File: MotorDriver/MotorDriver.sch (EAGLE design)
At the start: 21 parts, among them U1 ATTINY48/88-TQFP, U2 DRV8848

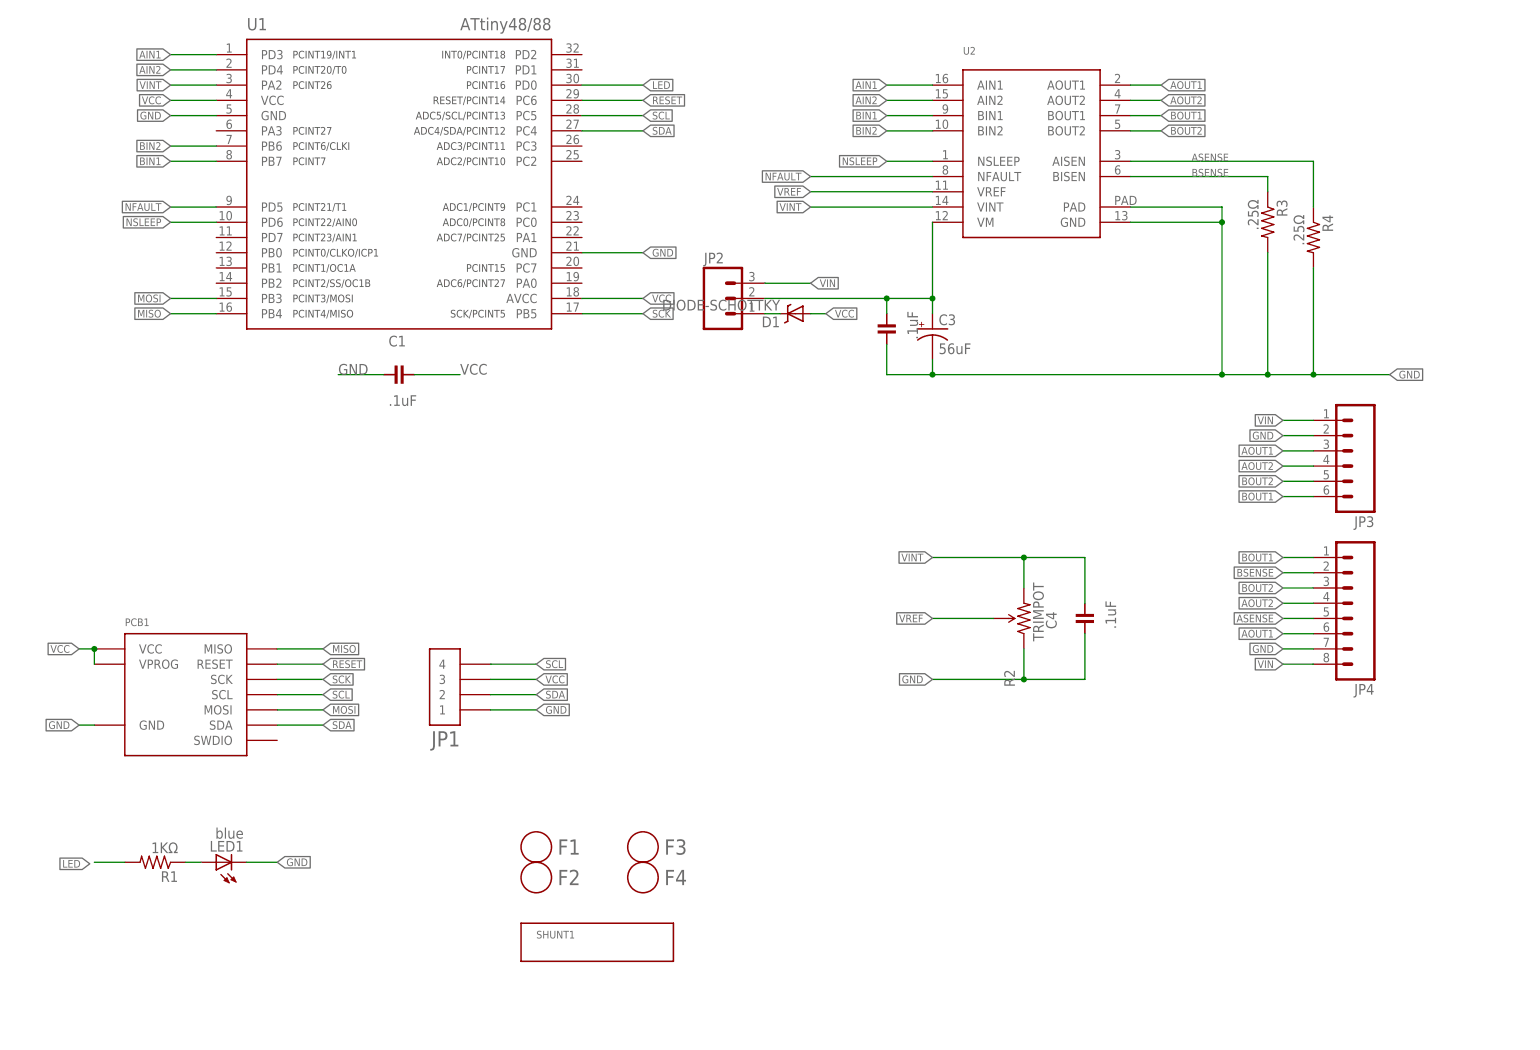
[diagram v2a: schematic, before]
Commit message: Check point of current PCB designs. Among other things I think this change includes rewiring of programming lines on many of the boards,.
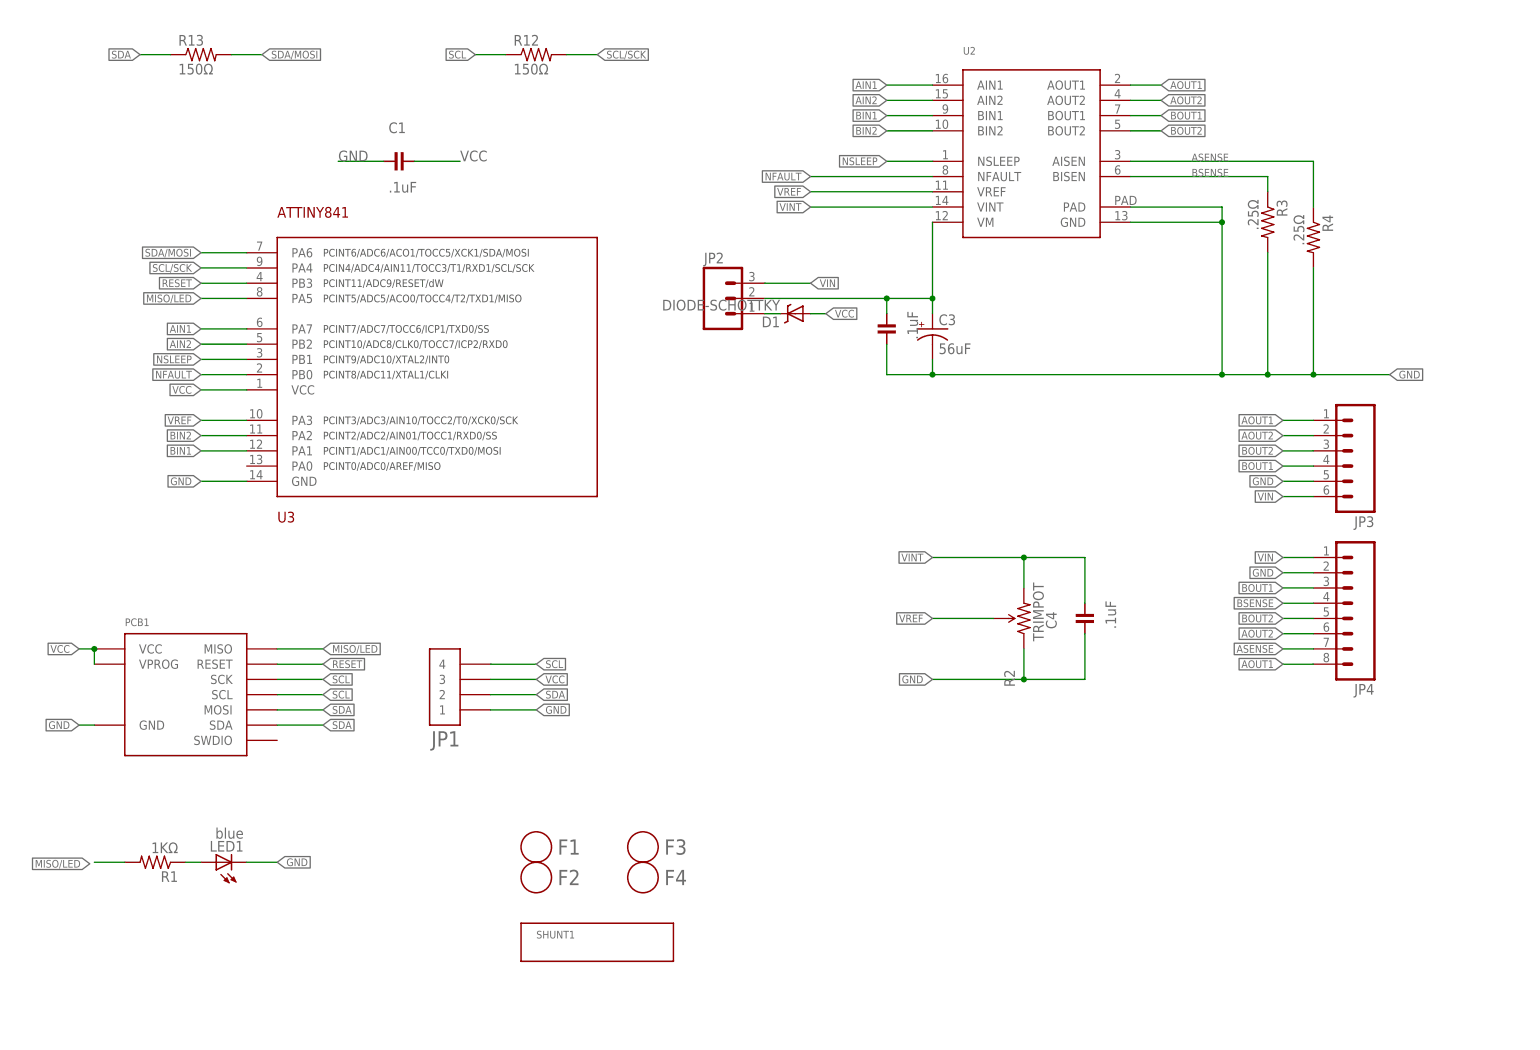
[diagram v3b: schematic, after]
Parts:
- removed U1: ATTINY48/88-TQFP, Modulo:ATTINY48/88-TQFP
- added R12, R13: 150Ω, Modulo:RESISTOR-150Ω
- added U3: ATTINY841, Modulo:ATTINY841
- JP4: BOM (none) -> EXCLUDE
- U2: PARTNUM DRV8848 -> (none)
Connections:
- removed net LED: R1.2, U1.PD0
- removed net MISO: PCB1.MISO, U1.PB4
- removed net MOSI: PCB1.MOSI, U1.PB3
- removed net SCK: PCB1.SCK, U1.PB5
- new net MISO/LED: PCB1.MISO, R1.2, U3.PA5
- new net SCL/SCK: R12.2, U3.PA4
- new net SDA/MOSI: R13.2, U3.PA6
- net AIN1: now also U3.PA7; no longer U1.PD3
- net AIN2: now also U3.PB2; no longer U1.PD4
- net AOUT1: now also JP3.1, JP4.8; no longer JP3.3, JP4.6
- net AOUT2: now also JP3.2, JP4.6; no longer JP3.4, JP4.4
- net ASENSE: now also JP4.7; no longer JP4.5
- net BIN1: now also U3.PA1; no longer U1.PB7
- net BIN2: now also U3.PA2; no longer U1.PB6
- net BOUT1: now also JP3.4, JP4.3; no longer JP3.6, JP4.1
- net BOUT2: now also JP3.3, JP4.5; no longer JP3.5, JP4.3
- net BSENSE: now also JP4.4; no longer JP4.2
- net GND: now also JP3.5, JP4.2, U3.GND; no longer JP3.2, JP4.7, U1.GND, U1.GND@1
- net NFAULT: now also U3.PB0; no longer U1.PD5
- net NSLEEP: now also U3.PB1; no longer U1.PD6
- net RESET: now also U3.PB3; no longer U1.PC6
- net SCL: now also PCB1.SCK, R12.1; no longer U1.PC5
- net SDA: now also PCB1.MOSI, R13.1; no longer U1.PC4
- net VCC: now also U3.VCC; no longer U1.AVCC, U1.VCC
- net VIN: now also JP3.6, JP4.1; no longer JP3.1, JP4.8
- net VINT: no longer U1.PA2
- net VREF: now also U3.PA3
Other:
- moved on the sheet: C1

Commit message: Various changes
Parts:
- removed JP4: (no value), SparkFun-Connectors:M08NO_SILK
- removed R2: TRIMPOT, Modulo:TRIMPOT
- added SJ1, SJ2, SJ3: SOLDERJUMPERNO, SparkFun-Passives:SOLDERJUMPERNO
- added U1: MCP4013, Modulo:MCP4013
- C4: value .1uF -> 10uF; device Modulo:CAPACITOR-.1UF -> Modulo:CAPACITOR-10UF
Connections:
- new net CS: U1.CS, U3.PA3
- new net UD: U1.UD, U3.PA0
- net AOUT1: no longer JP4.8
- net AOUT2: no longer JP4.6
- net ASENSE: now also SJ3.2; no longer JP4.7
- net BOUT1: no longer JP4.3
- net BOUT2: no longer JP4.5
- net BSENSE: now also SJ2.2; no longer JP4.4
- net GND: now also SJ2.1, SJ3.1, U1.GND; no longer JP4.2, R2.CCW
- net VCC: now also U1.VCC
- net VIN: no longer JP4.1
- net VINT: now also SJ1.1, U1.A; no longer R2.CW
- net VREF: now also SJ1.2, U1.W; no longer R2.WIPER, U3.PA3

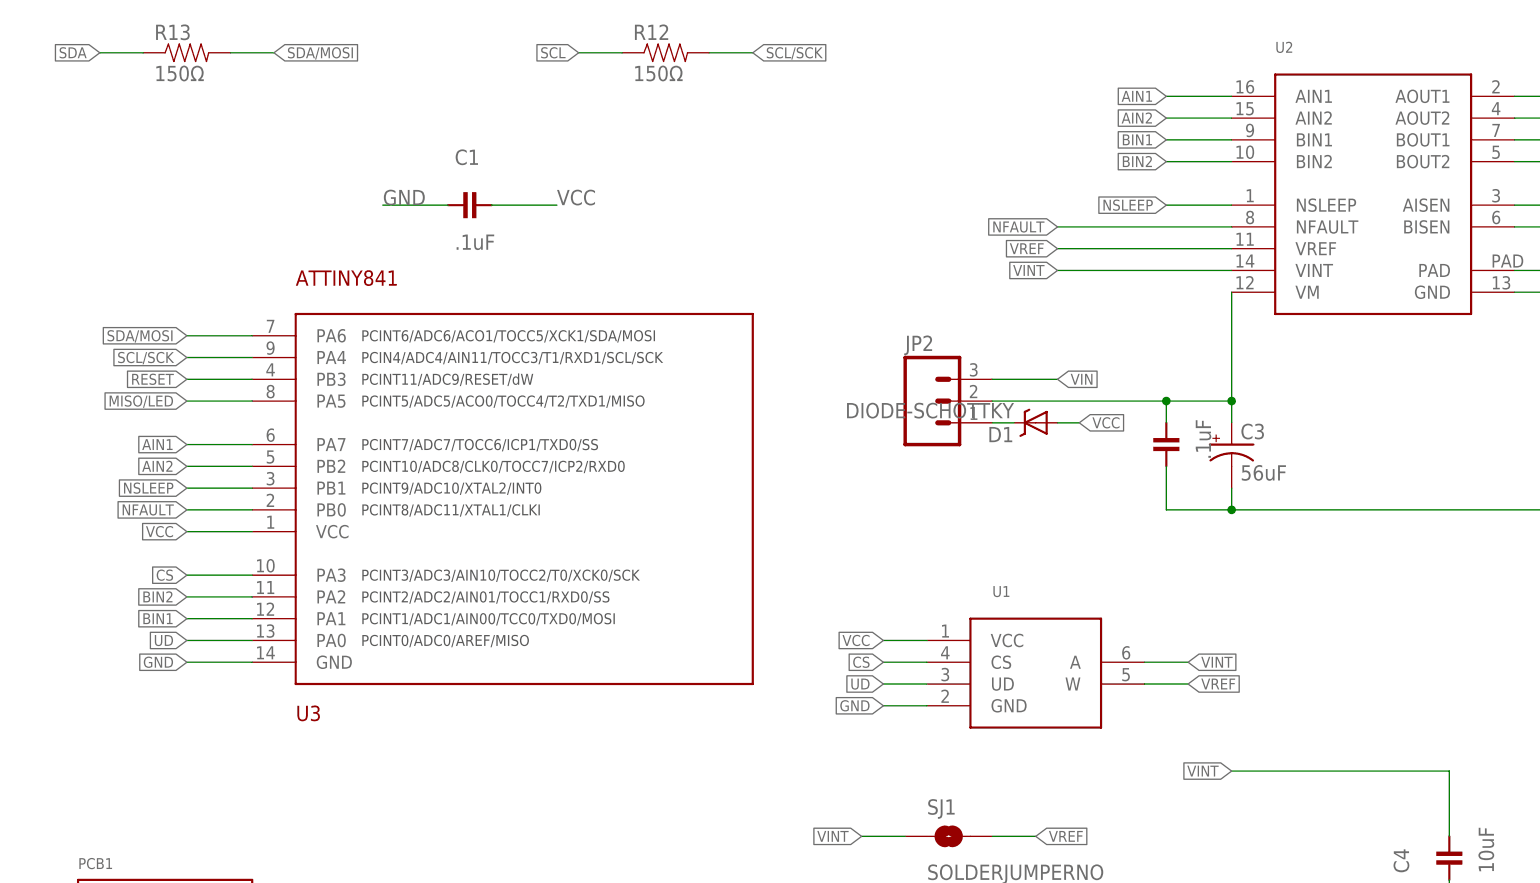
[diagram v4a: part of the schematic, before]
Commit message: Various small tweaks based on testing and feedback from manufacturer.
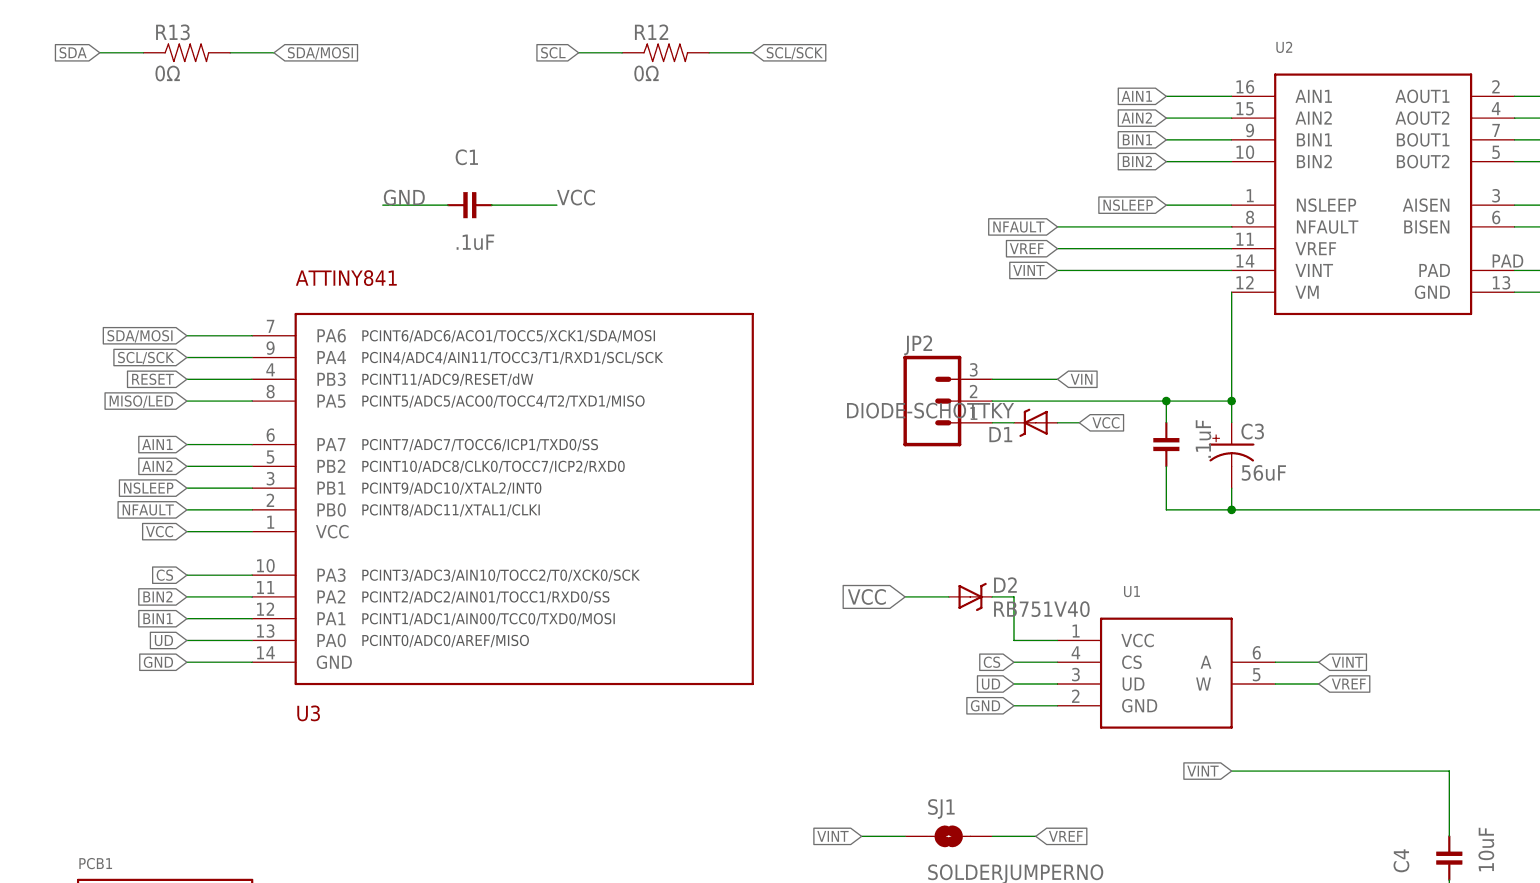
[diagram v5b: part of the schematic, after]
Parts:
- added D2: RB751V40, Modulo:DIODE-SCHOTTKY-BAT60A
- R12, R13: value 150Ω -> 0Ω; device Modulo:RESISTOR-150Ω -> Modulo:RESISTOR-0Ω
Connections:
- new net N$2: D2.C, U1.VCC
- net VCC: now also D2.A; no longer U1.VCC
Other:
- moved on the sheet: U1
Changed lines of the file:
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@@
 <part name="D1" library="Modulo" deviceset="DIODE-SCHOTTKY" device="" value="DIODE-SCHOTTKY"/>
 <part name="U3" library="Modulo" deviceset="ATTINY841" device=""/>
-<part name="R12" library="Modulo" deviceset="RESISTOR" device="-150Ω" value="150Ω"/>
-<part name="R13" library="Modulo" deviceset="RESISTOR" device="-150Ω" value="150Ω"/>
+<part name="R12" library="Modulo" deviceset="RESISTOR" device="-0Ω" value="0Ω"/>
+<part name="R13" library="Modulo" deviceset="RESISTOR" device="-0Ω" value="0Ω"/>
 <part name="U1" library="Modulo" deviceset="MCP4013" device=""/>
 <part name="SJ1" library="SparkFun-Passives" deviceset="SOLDERJUMPER" device="NO">
@@
 <attribute name="BOM" value="EXCLUDE"/>
 </part>
+<part name="D2" library="Modulo" deviceset="DIODE-SCHOTTKY" device="-BAT60A" value="RB751V40">
+<attribute name="PARTNUM" value="RB751V40"/>
+</part>
 </parts>
 <sheets>
@@
 <instance part="R12" gate="G$1" x="86.36" y="162.56"/>
 <instance part="R13" gate="G$1" x="30.48" y="162.56"/>
-<instance part="U1" gate="G$1" x="127" y="91.44"/>
+<instance part="U1" gate="G$1" x="142.24" y="91.44"/>
 <instance part="SJ1" gate="1" x="119.38" y="71.12">
 <attribute name="BOM" x="119.38" y="71.12" size="1.27" layer="96" display="off"/>
@@
 <attribute name="BOM" x="220.98" y="124.46" size="1.27" layer="96" rot="R90" display="off"/>
 </instance>
+<instance part="D2" gate="G$1" x="121.92" y="99.06"/>
 </instances>
 <busses>
@@
 </segment>
 <segment>
-<pinref part="U1" gate="G$1" pin="VCC"/>
-<wire x1="116.84" y1="93.98" x2="111.76" y2="93.98" width="0.1524" layer="91"/>
-<label x="111.76" y="93.98" size="1.27" layer="95" rot="R180" xref="yes"/>
+<pinref part="D2" gate="G$1" pin="A"/>
+<wire x1="119.38" y1="99.06" x2="114.3" y2="99.06" width="0.1524" layer="91"/>
+<label x="114.3" y="99.06" size="1.778" layer="95" rot="R180" xref="yes"/>
 </segment>
 </net>
@@
 <segment>
 <pinref part="U1" gate="G$1" pin="GND"/>
-<wire x1="116.84" y1="86.36" x2="111.76" y2="86.36" width="0.1524" layer="91"/>
-<label x="111.76" y="86.36" size="1.27" layer="95" rot="R180" xref="yes"/>
+<wire x1="132.08" y1="86.36" x2="127" y2="86.36" width="0.1524" layer="91"/>
+<label x="127" y="86.36" size="1.27" layer="95" rot="R180" xref="yes"/>
 </segment>
 </net>
@@
 <segment>
 <pinref part="U1" gate="G$1" pin="W"/>
-<wire x1="142.24" y1="88.9" x2="147.32" y2="88.9" width="0.1524" layer="91"/>
-<label x="147.32" y="88.9" size="1.27" layer="95" xref="yes"/>
+<wire x1="157.48" y1="88.9" x2="162.56" y2="88.9" width="0.1524" layer="91"/>
+<label x="162.56" y="88.9" size="1.27" layer="95" xref="yes"/>
 </segment>
 <segment>
@@
 <segment>
 <pinref part="U1" gate="G$1" pin="A"/>
-<wire x1="142.24" y1="91.44" x2="147.32" y2="91.44" width="0.1524" layer="91"/>
-<label x="147.32" y="91.44" size="1.27" layer="95" xref="yes"/>
+<wire x1="157.48" y1="91.44" x2="162.56" y2="91.44" width="0.1524" layer="91"/>
+<label x="162.56" y="91.44" size="1.27" layer="95" xref="yes"/>
 </segment>
 <segment>
@@
 <segment>
 <pinref part="U1" gate="G$1" pin="CS"/>
-<wire x1="116.84" y1="91.44" x2="111.76" y2="91.44" width="0.1524" layer="91"/>
-<label x="111.76" y="91.44" size="1.27" layer="95" rot="R180" xref="yes"/>
+<wire x1="132.08" y1="91.44" x2="127" y2="91.44" width="0.1524" layer="91"/>
+<label x="127" y="91.44" size="1.27" layer="95" rot="R180" xref="yes"/>
 </segment>
 </net>
@@
 <segment>
 <pinref part="U1" gate="G$1" pin="UD"/>
-<wire x1="116.84" y1="88.9" x2="111.76" y2="88.9" width="0.1524" layer="91"/>
-<label x="111.76" y="88.9" size="1.27" layer="95" rot="R180" xref="yes"/>
-</segment>
-</net>
+<wire x1="132.08" y1="88.9" x2="127" y2="88.9" width="0.1524" layer="91"/>
+<label x="127" y="88.9" size="1.27" layer="95" rot="R180" xref="yes"/>
+</segment>
+</net>
+<net name="N$2" class="0">
+<segment>
+<pinref part="D2" gate="G$1" pin="C"/>
+<wire x1="124.46" y1="99.06" x2="127" y2="99.06" width="0.1524" layer="91"/>
+<wire x1="127" y1="99.06" x2="127" y2="93.98" width="0.1524" layer="91"/>
+<pinref part="U1" gate="G$1" pin="VCC"/>
+<wire x1="127" y1="93.98" x2="132.08" y2="93.98" width="0.1524" layer="91"/>
+</segment>
+</net>
